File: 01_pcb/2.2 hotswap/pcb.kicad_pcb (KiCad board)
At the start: 2 copper layers, 251.2 x 75 mm, 128 parts, among them J1 TYPE-C-31-M12_13, J2 AVR-ISP-6_mod, J3 Conn_01x05_Female, J8 4PIN, K1 KEYSW, K10 KEYSW, K12 KEYSW, K13 KEYSW, K14 KEYSW, K15 KEYSW, K16 KEYSW, K17 KEYSW, K18 KEYSW, K19 KEYSW, K2 KEYSW, K20 KEYSW, K21 KEYSW, K23 KEYSW, K24 KEYSW, K25 KEYSW, K26 KEYSW, K27 KEYSW, K28 KEYSW, K29 KEYSW, K3 KEYSW, K30 KEYSW, K31 KEYSW, K32 KEYSW, K33 KEYSW, K34 KEYSW, K36 KEYSW, K37 KEYSW, K38 KEYSW, K39 KEYSW, K4 KEYSW, K42 KEYSW, K43 KEYSW, K44 KEYSW, K45 KEYSW, K46 KEYSW, K47 KEYSW, K48 KEYSW, K49 KEYSW, K5 KEYSW, K50 KEYSW, K51 KEYSW, K52 KEYSW, K6 KEYSW, K7 KEYSW, K8 KEYSW, K9 KEYSW, SW1 SW_PUSH, U1 ATMEGA32U4, U2 PRTR5V0U2X, Y1 16MHz

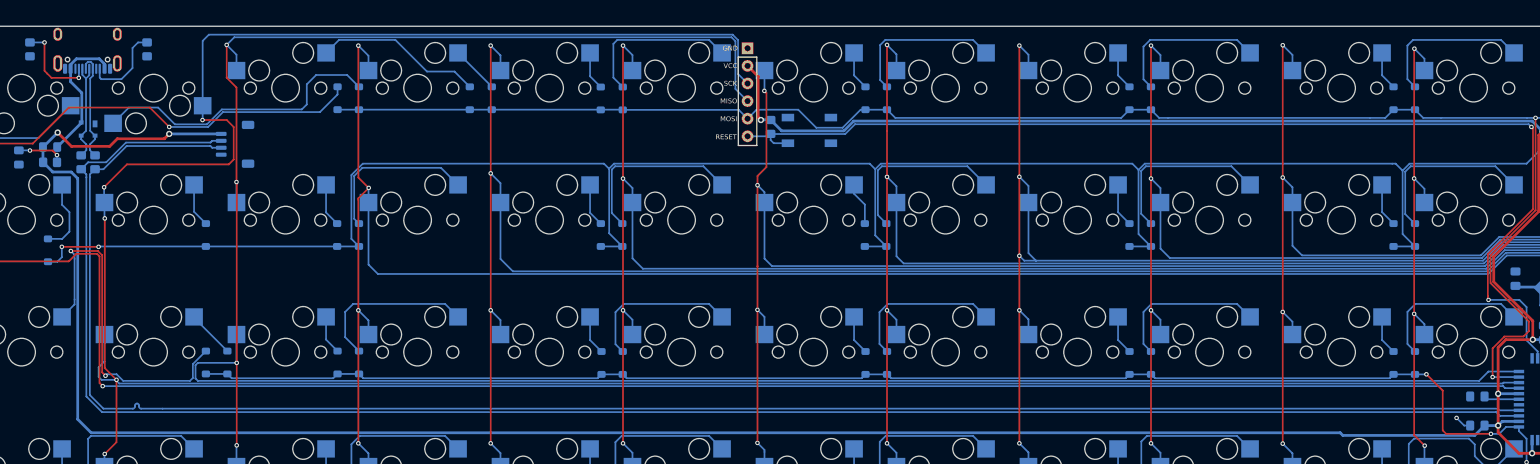
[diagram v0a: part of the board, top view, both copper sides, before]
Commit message: moved USB port data line resistors
also added 3d models, etc.
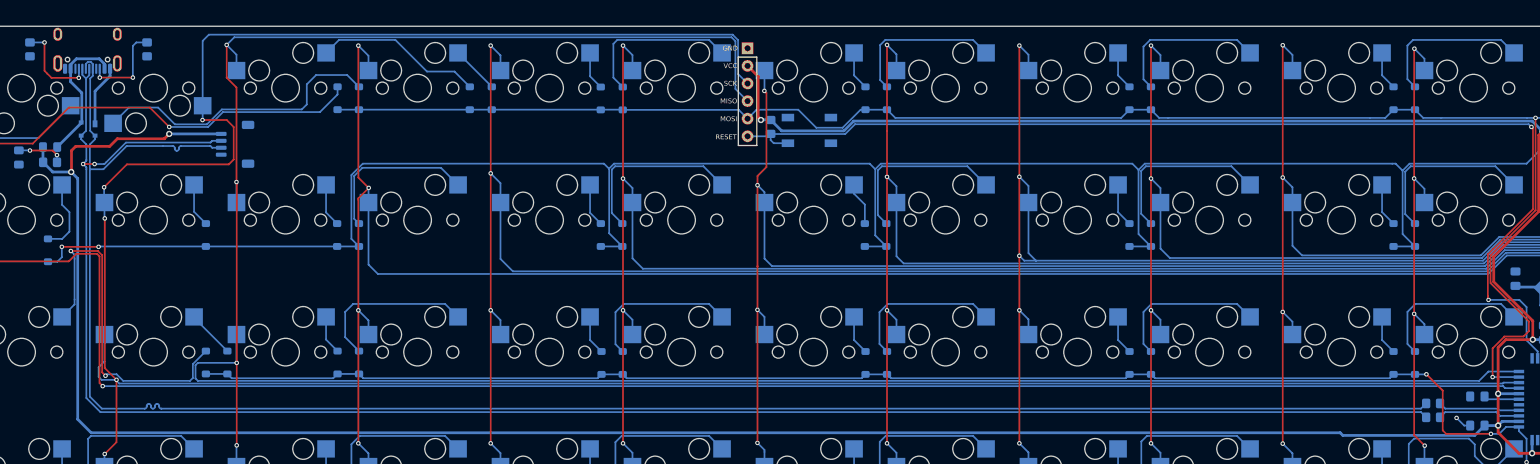
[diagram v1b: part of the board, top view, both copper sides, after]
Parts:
- moved R2 198.5 mm to (290.6, 100.7), turned to 180 degrees
- moved R3 196.2 mm to (290.6, 98.7), turned to 180 degrees
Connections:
- net col1 renamed col1/sck
- net col2 renamed col2/miso
- net row0 renamed row0/mosi
- J8 pad 2: D- -> DBUS-
- J8 pad 3: D+ -> DBUS+
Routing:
- net DBUS+: track 15.8 -> 267.1 mm
- net D-: track 263.0 -> 11.9 mm
- net DBUS-: track 16.3 -> 267.2 mm, vias 0 -> 2
- net D+: track 260.7 -> 11.8 mm
- net GND: track 11.6 -> 21.0 mm
- net VCC: track 507.1 -> 504.7 mm
- net Net-(J1-CC2): track 12.6 -> 13.4 mm, vias 0 -> 2
